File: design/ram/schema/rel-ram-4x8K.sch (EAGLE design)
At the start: 6 parts

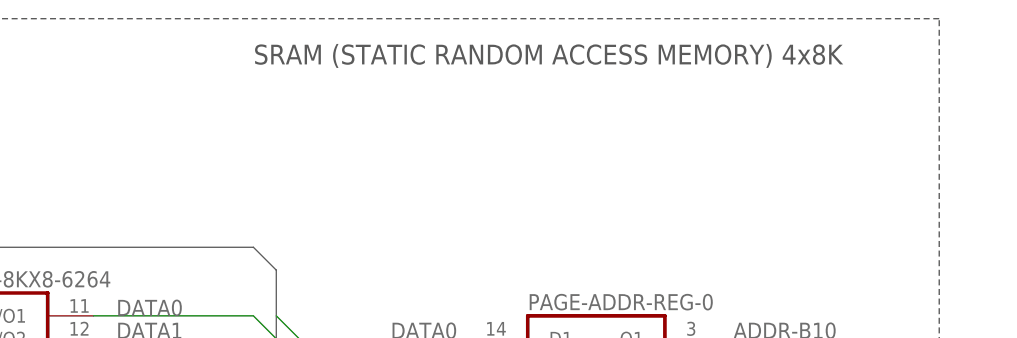
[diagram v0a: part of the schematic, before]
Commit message: Aligned titles size for all schemas
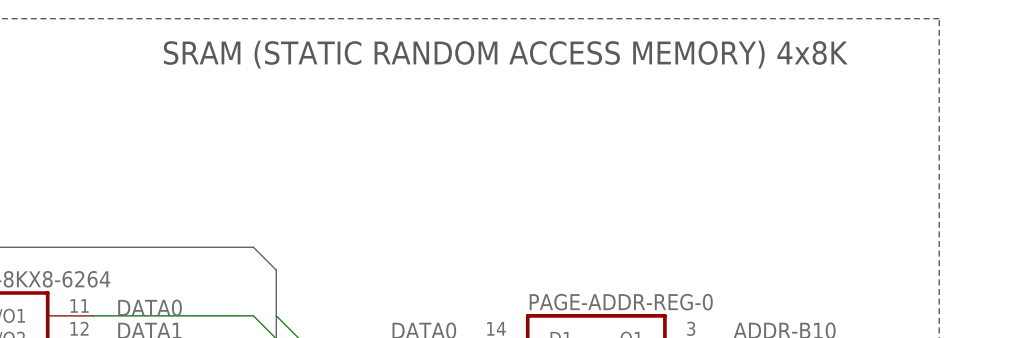
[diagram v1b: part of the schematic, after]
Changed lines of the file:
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@@
 <?xml version="1.0" encoding="utf-8"?>
 <!DOCTYPE eagle SYSTEM "eagle.dtd">
-<eagle version="9.6.2">
+<eagle version="9.1.3">
 <drawing>
 <settings>
@@
 <sheet>
 <plain>
-<text x="101.6" y="142.24" size="2.1844" layer="97">SRAM (STATIC RANDOM ACCESS MEMORY) 4x8K</text>
+<text x="91.44" y="142.24" size="2.54" layer="97">SRAM (STATIC RANDOM ACCESS MEMORY) 4x8K</text>
 <wire x1="-38.1" y1="147.32" x2="-38.1" y2="-17.78" width="0.1524" layer="97" style="shortdash"/>
 <wire x1="-38.1" y1="-17.78" x2="177.8" y2="-17.78" width="0.1524" layer="97" style="shortdash"/>
